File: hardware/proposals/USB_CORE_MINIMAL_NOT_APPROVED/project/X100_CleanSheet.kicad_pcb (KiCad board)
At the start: 4 copper layers, 45 x 45 mm, 240 parts, among them J401 124019772112A, J501 1040310811, J601 SM04B-GHS-TB(LF)(SN), J701 SM06B-GHS-TB(LF)(SN), J702 SM06B-GHS-TB(LF)(SN), J703 SM06B-GHS-TB(LF)(SN), J704 SM04B-GHS-TB(LF)(SN), J801 OUT1 /GND, J802 OUT2 /GND, J803 OUT3 /GND, J804 OUT4 /GND, J805 OUT5 /GND, J806 OUT6 /GND, J807 SWD:1REF2GND3IO4CLK5NRST, J808 BATTERY/bench3S-6S ONLY, J809 CURRENT monitor only, Q101 DMP6023LSS-13, Q102 BSS138LT1G CAN shutdown, U101 TPS54360BDDAR, U102 AP63203WU-7, U103 TPS7A2033PDBVR, U104 TPS2553DBVR, U105 TPS2116DRLR, U106 TPS2553DBVR, U107 TPS22918DBVR core controlled 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, U108 TPS22918DBVR, U109 SN74CB3Q3245PWR, U110 TLV6700DDCR, U111 SN74LVC1G00DBVR, U112 TMUX1219DBVR ILIM selector, U114 SN74AUP1G32DBVR core sensor EN, U201 STM32H743VIT6, U301 BMI088, U302 SPL06-001, U401 TPD2E2U06QDBZRQ1, U402 SN74LVC1G17DBVR, U403 TPD2E2U06QDBZRQ1, U404 TPD2E2U06QDBZRQ1, U601 TCAN3414DR, U801 TMUX1511PWR, Y201 8.000MHz /CL20pF

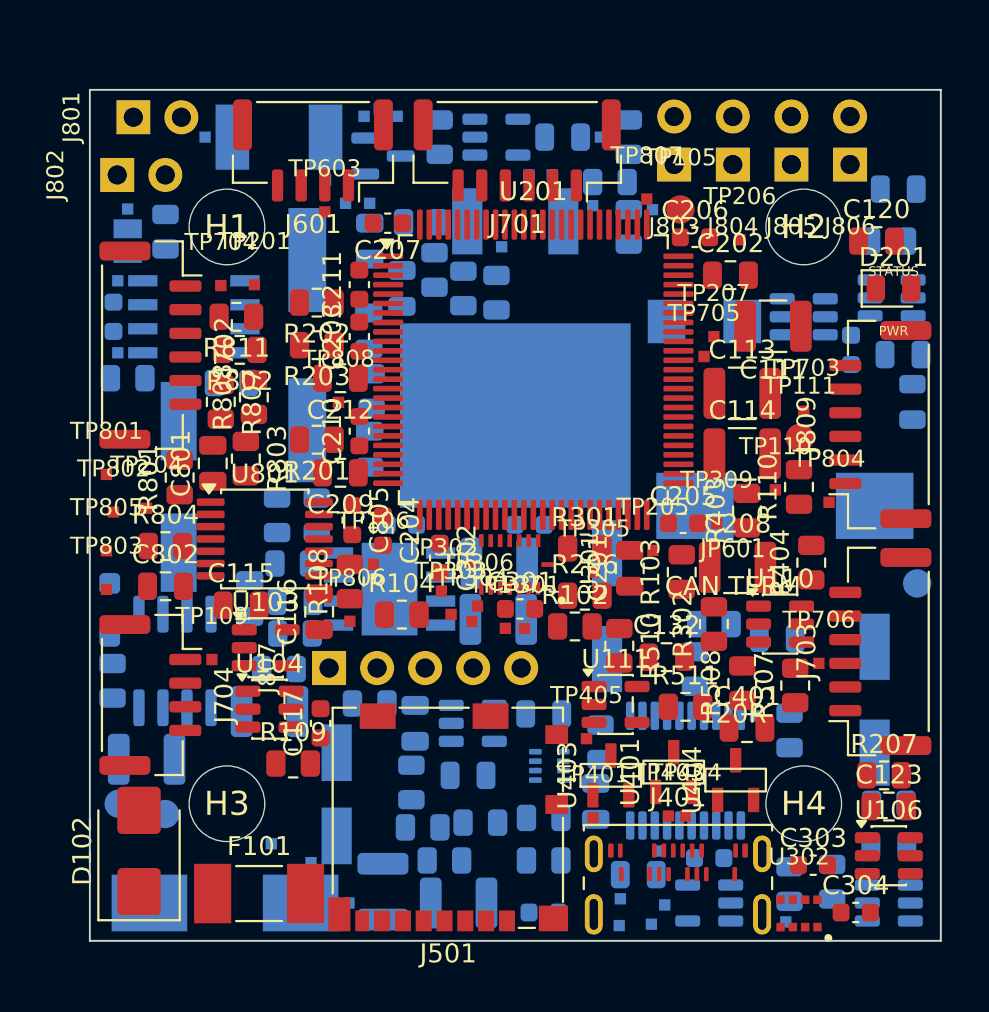
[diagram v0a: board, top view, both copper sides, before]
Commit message: Clear all four 7mm mounting envelopes in the complete USB layout
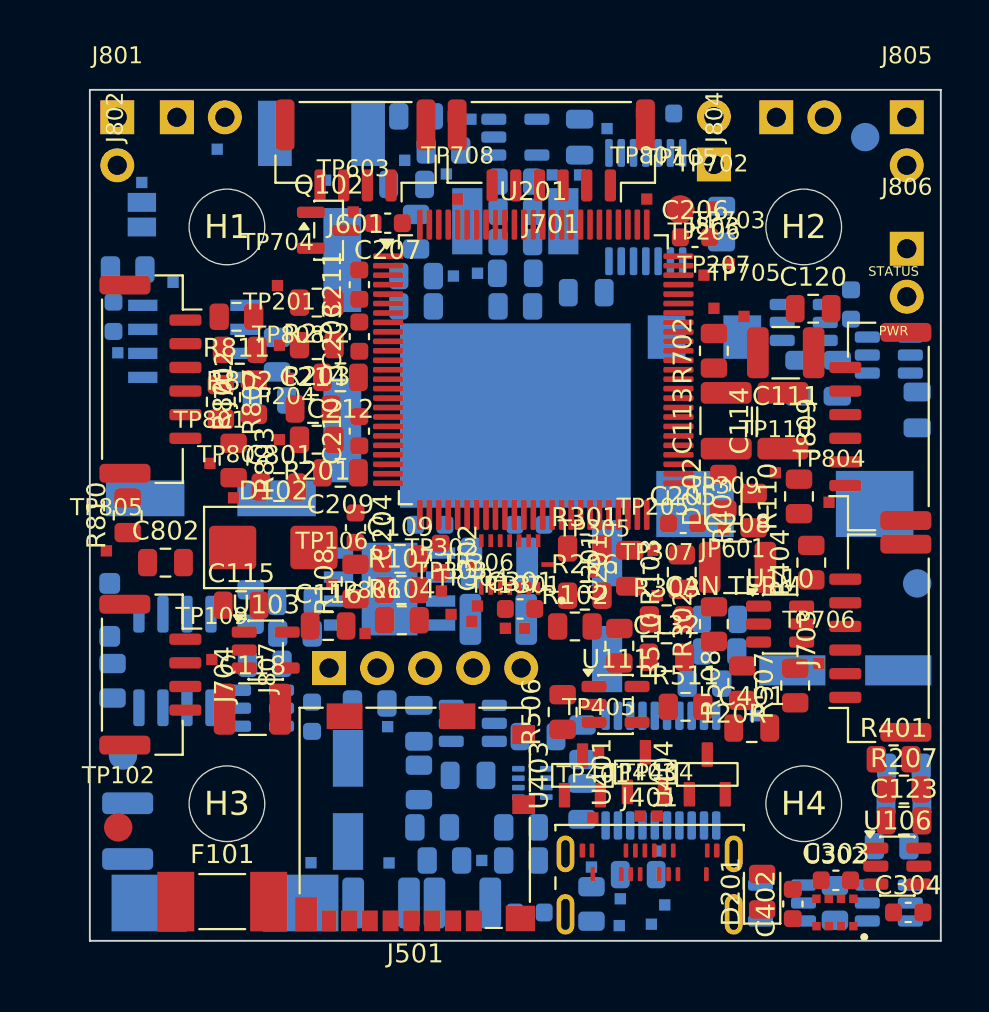
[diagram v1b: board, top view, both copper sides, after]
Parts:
- C109, C118, C214, C402, D202, Q102, R107, R303, R401, R506, R702, R810, TP102, TP307, TP702, TP708: moved to F.Cu
- C117, C202, C805, R109, R804, R808, TP111, TP803, U104, U801: moved to B.Cu
- moved R304 35.9 mm to (104.0, 120.5)
- moved TP308 34.9 mm to (104.0, 118.6)
- moved D201 32.6 mm to (113.0, 119.9), turned to 90 degrees
- moved C805 26.9 mm to (107.6, 78.8), turned to 180 degrees
- moved U801 26.7 mm to (106.9, 83.7), turned to 90 degrees
- moved TP803 25.8 mm to (98.0, 87.2)
- moved R804 25.6 mm to (100.0, 84.0)
- moved R303 25.6 mm to (108.0, 105.5), turned to 0 degrees
- moved R810 22.8 mm to (79.5, 100.0)
- moved TP307 18.5 mm to (107.5, 104.2)
- moved D102 17.6 mm to (87.2, 101.7), turned to 0 degrees
- moved R805 16.7 mm to (94.8, 85.0)
- moved TP111 16.3 mm to (118.5, 80.0)
- moved R702 15.4 mm to (110.5, 91.3)
- moved R808 14.6 mm to (100.0, 89.0), turned to 0 degrees
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
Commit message: Clear MCU-IMU routing channel in the complete USB candidate
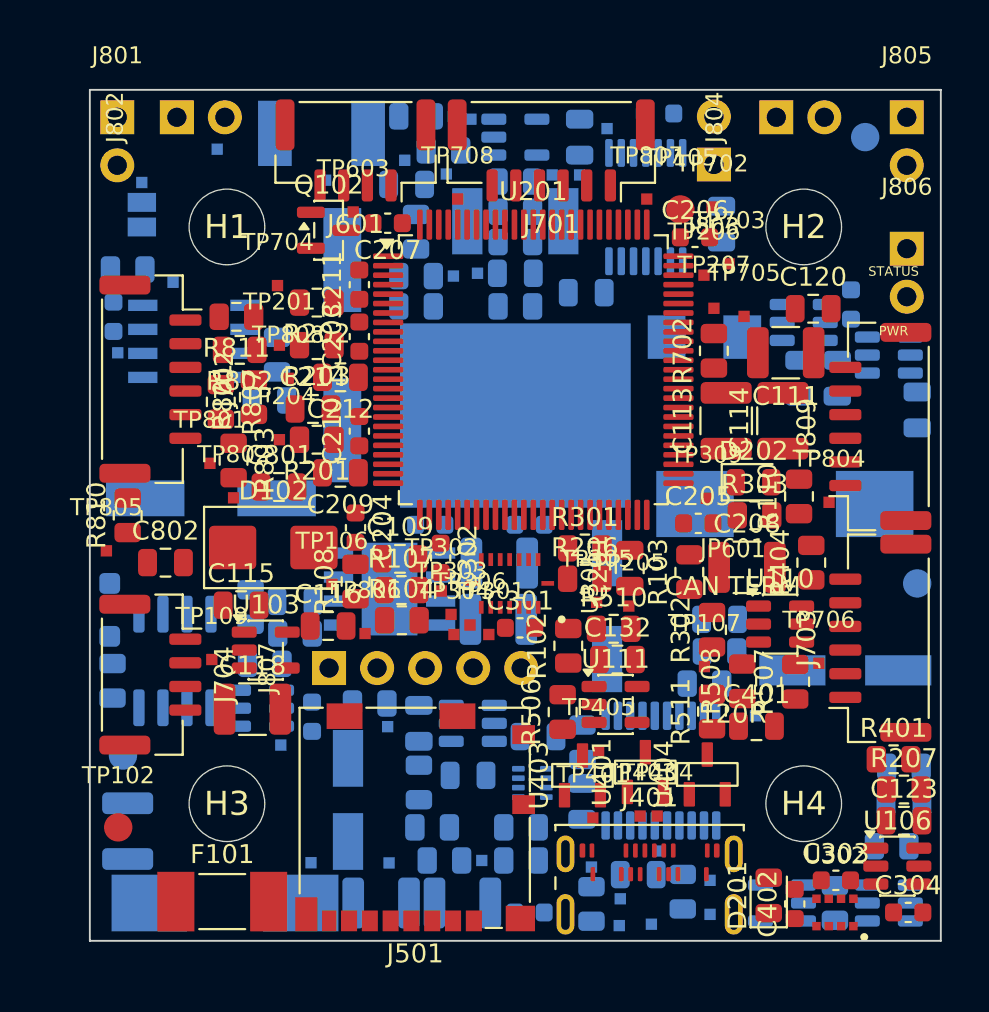
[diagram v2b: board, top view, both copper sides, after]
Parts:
- R403, TP110, TP307: moved to B.Cu
- moved TP110 29.9 mm to (87.6, 112.2)
- moved R403 20.5 mm to (108.8, 119.9)
- moved TP307 15.3 mm to (110.3, 119.3)
- moved TP107 10.7 mm to (110.0, 108.0)
- moved R303 7.20 mm to (112.7, 100.0)
- moved TP205 3.21 mm to (106.0, 104.8)
- moved C132 2.60 mm to (105.4, 107.6)
- moved TP402 2.45 mm to (110.3, 121.1)
- moved TP301 1.90 mm to (98.6, 106.3)
- moved TP309 1.86 mm to (110.1, 99.1)
- moved D202 1.68 mm to (112.6, 98.2), turned to 0 degrees
- moved TP305 1.61 mm to (104.3, 104.6)
- moved R511 1.42 mm to (110.4, 110.4), turned to 90 degrees
- moved TP304 1.18 mm to (96.8, 106.3)
- moved R102 1.08 mm to (102.8, 106.9), turned to 90 degrees
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
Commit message: Route main Buck controls and ground in the unified X100 candidate
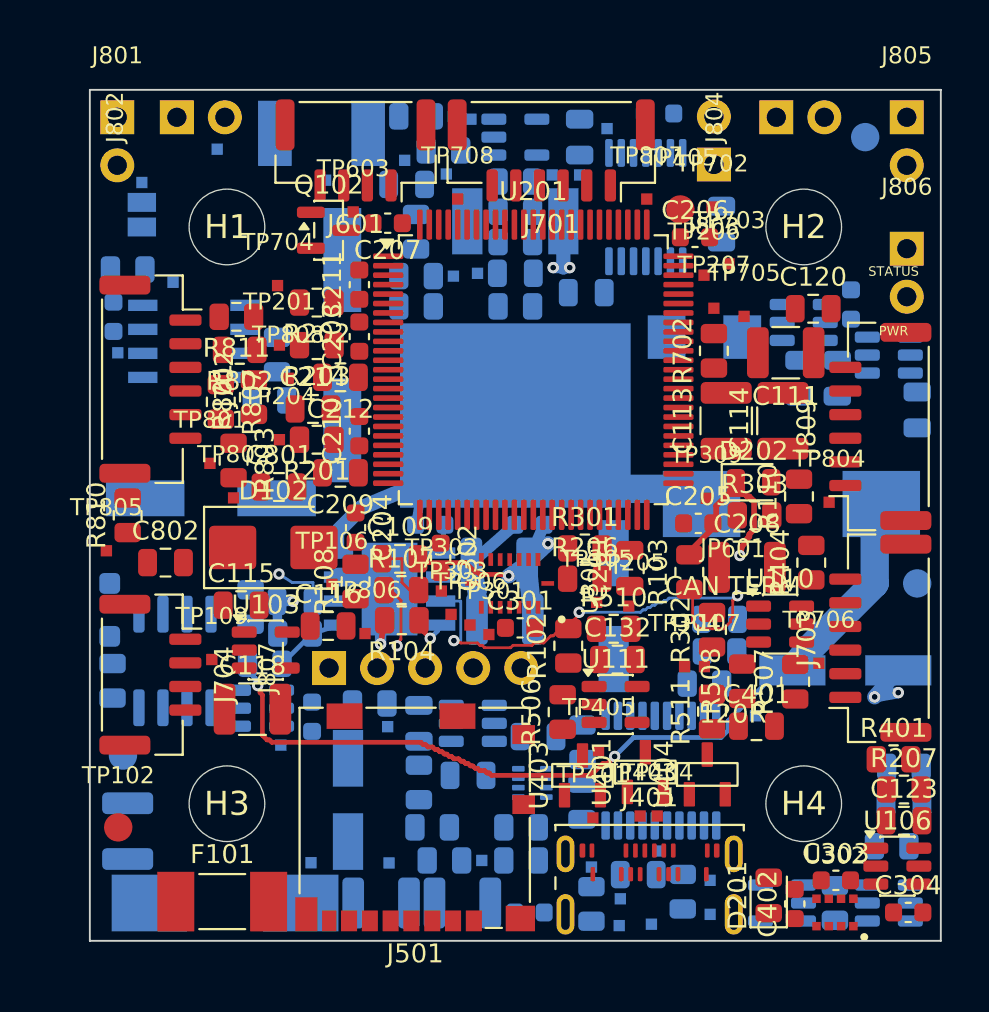
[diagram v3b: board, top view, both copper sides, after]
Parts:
- moved TP304 12.3 mm to (109.0, 108.0)
- moved C102 0.35 mm to (99.5, 105.5)
- moved C121 0.35 mm to (105.2, 104.8)
- moved L101 0.35 mm to (114.6, 99.4)
- turned R104 to 180 degrees
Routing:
- net 5V_MAIN: track 0.00 -> 46.1 mm, vias 0 -> 2
- net GND: track 0.00 -> 35.7 mm, vias 0 -> 9
- net MAIN_EN: track 0.00 -> 25.5 mm, vias 0 -> 3
- net MAIN_COMP: track 0.00 -> 15.9 mm, vias 0 -> 2
- net MAIN_SW: track 0.00 -> 11.8 mm
- net VBAT_PROTECTED: track 0.00 -> 7.86 mm
- net MAIN_FB: track 0.00 -> 3.72 mm
- net MAIN_COMP_RC: track 0.00 -> 3.35 mm
- net MAIN_RT: track 0.00 -> 2.06 mm, vias 0 -> 1
- net MAIN_BOOT: track 0.00 -> 1.51 mm
- added copper zone on In1.Cu, net GND

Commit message: Connect the X100 protected battery input and verify its copper plane
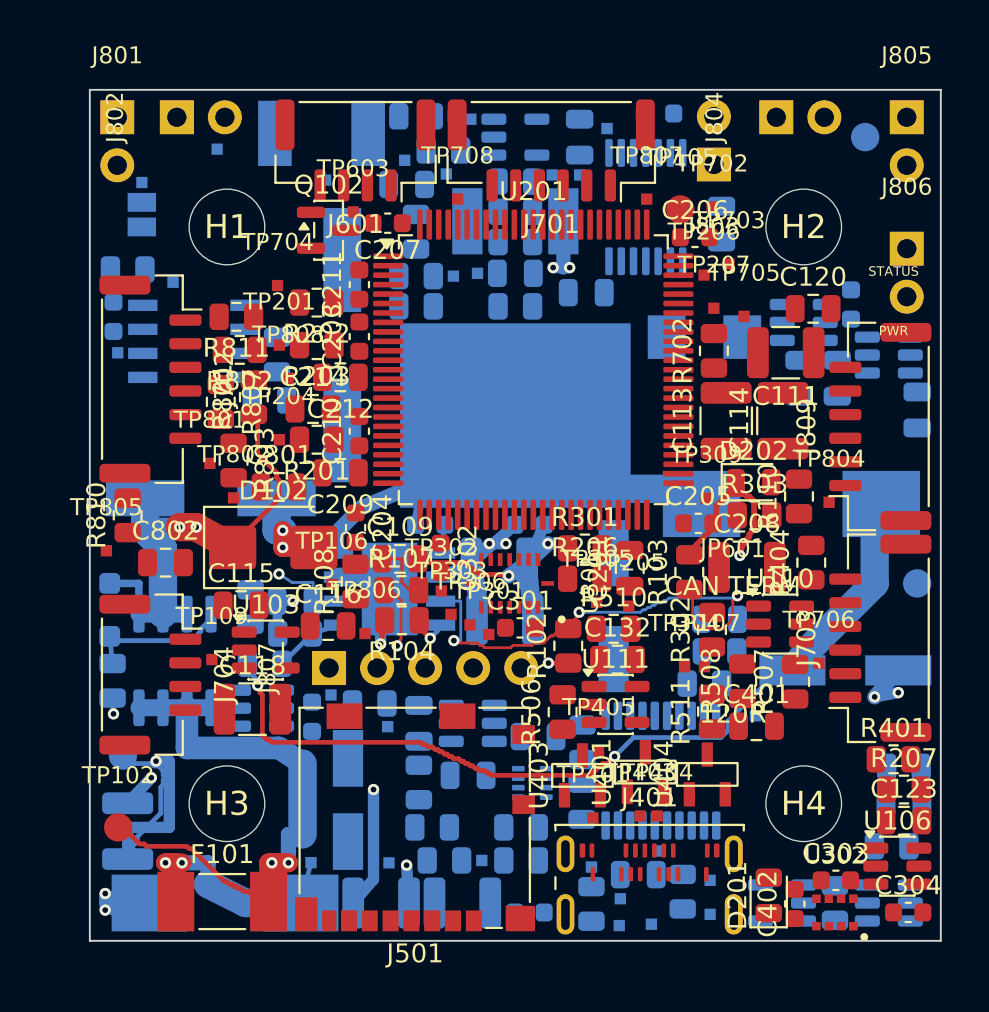
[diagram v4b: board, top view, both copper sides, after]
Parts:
- moved TP101 4.13 mm to (89.2, 118.4)
- moved TP507 4.13 mm to (93.3, 118.4)
- moved TP110 3.75 mm to (90.2, 109.5)
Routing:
- net VBAT_PROTECTED: track 7.86 -> 61.0 mm, vias 0 -> 7
- net VBAT_FUSED: track 0.00 -> 32.7 mm, vias 0 -> 2
- net VBAT_RAW: track 0.00 -> 15.1 mm, vias 0 -> 2
- net GND: track 35.7 -> 48.7 mm, vias 9 -> 16
- net RP_GATE: track 0.00 -> 7.70 mm
- added copper zone on In2.Cu, net VBAT_PROTECTED

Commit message: Route 5V main distribution and preserve isolated feedback sense
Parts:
- R510: moved to B.Cu
- moved R510 10.2 mm to (107.0, 96.0), turned to 90 degrees
- moved R506 5.16 mm to (105.2, 106.0), turned to 0 degrees
- turned C118 to 180 degrees
- turned U104 to 180 degrees
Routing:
- net 5V_MAIN: track 46.1 -> 120.9 mm, vias 2 -> 9
- net CORE_PWR_PRIORITY: track 0.00 -> 13.5 mm
- net GND: track 48.7 -> 58.8 mm, vias 16 -> 21

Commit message: Route external 5V protection and restore input copper capacity
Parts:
- TP110: moved to F.Cu
- moved TP110 12.8 mm to (103.0, 108.8), turned to 180 degrees
- moved R105 0.38 mm to (86.4, 107.8)
- turned R109 to -90 degrees
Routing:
- net EXT_SWITCH_OUT: track 0.00 -> 54.6 mm, vias 0 -> 5
- net EXT_FAULT: track 0.00 -> 37.3 mm, vias 0 -> 3
- net EXT_ILIM: track 0.00 -> 10.6 mm, vias 0 -> 2
- net GND: track 58.8 -> 65.6 mm
- net MAIN_COMP: track 15.9 -> 12.3 mm
- net 5V_MAIN: track 120.9 -> 122.8 mm, vias 9 -> 10
- net MAIN_FB: track 3.72 -> 5.13 mm

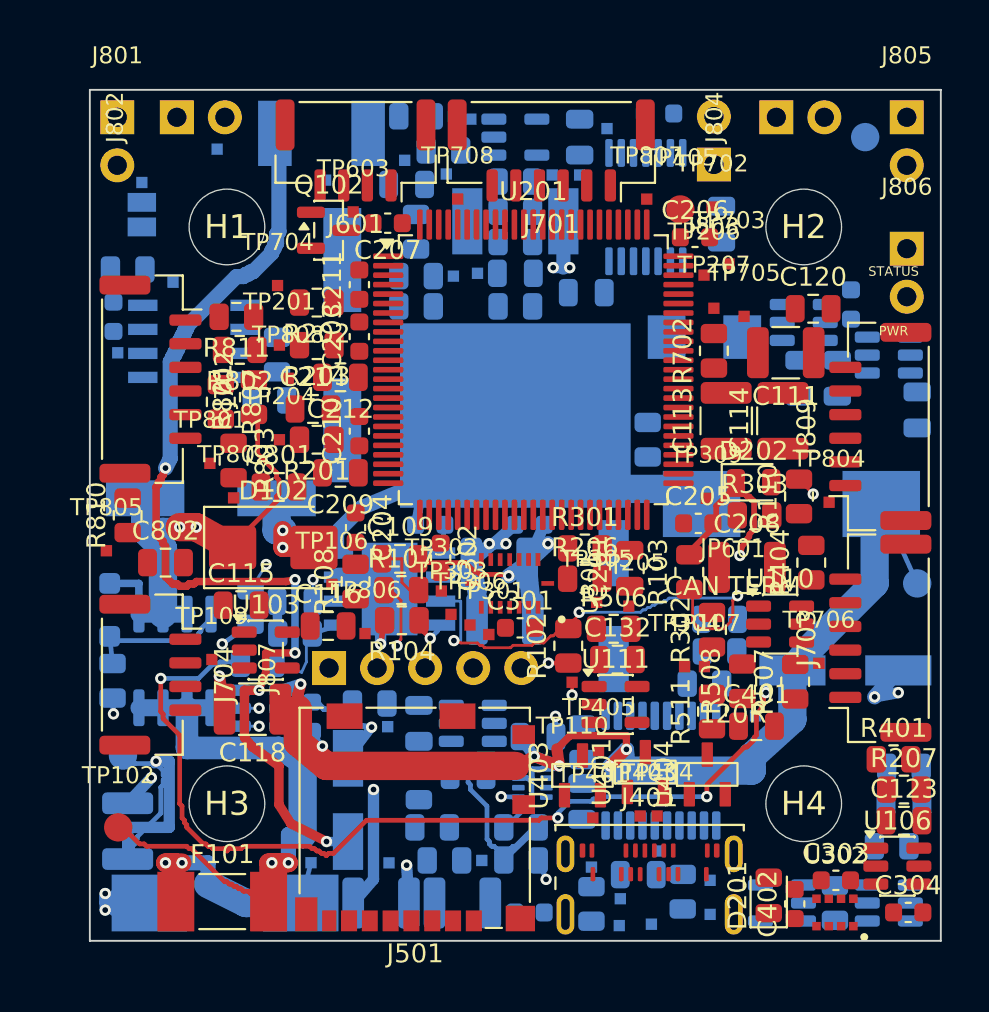
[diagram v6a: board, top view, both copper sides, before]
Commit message: Route core power mux and local 3V3 regulator supply
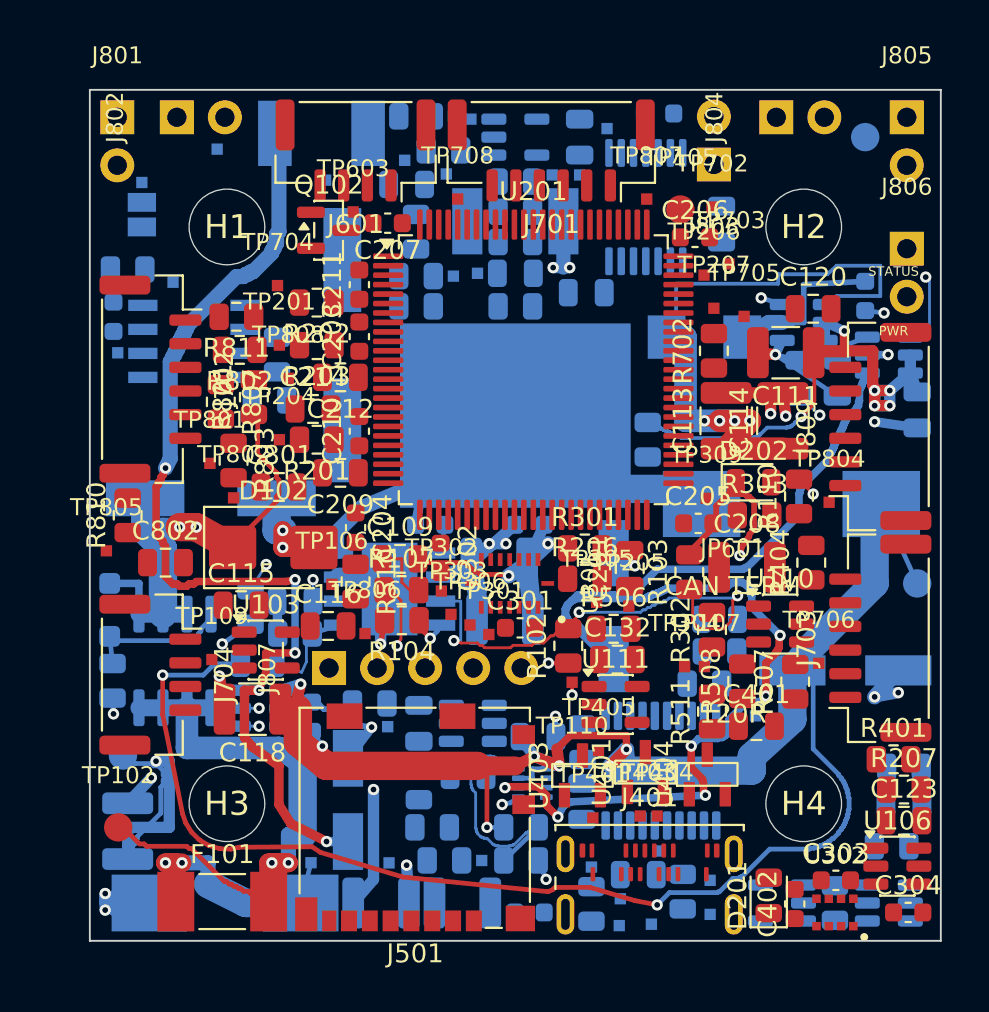
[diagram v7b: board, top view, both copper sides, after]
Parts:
- R108: moved to B.Cu
- R510: moved to F.Cu
- moved R108 17.2 mm to (107.0, 96.0), turned to -90 degrees
- moved R510 17.2 mm to (91.5, 103.5), turned to -90 degrees
- moved C112 0.87 mm to (118.5, 88.4)
- turned U102 to 180 degrees
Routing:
- net 5V_CORE_MUX: track 0.00 -> 74.8 mm, vias 0 -> 6
- net 3V3_MCU: track 0.00 -> 35.6 mm, vias 0 -> 4
- net 5V_CORE: track 0.00 -> 31.8 mm, vias 0 -> 6
- net GND: track 65.6 -> 82.0 mm, vias 21 -> 27
- net CORE_SLEW: track 0.00 -> 15.7 mm, vias 0 -> 2
- net MCU_BOOT: track 0.00 -> 8.72 mm, vias 0 -> 2
- net MCU_SW: track 0.00 -> 8.70 mm
- net 5V_MAIN: track 122.8 -> 131.2 mm, vias 10 -> 9

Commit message: Route first MCU supply pass and expose remaining power islands
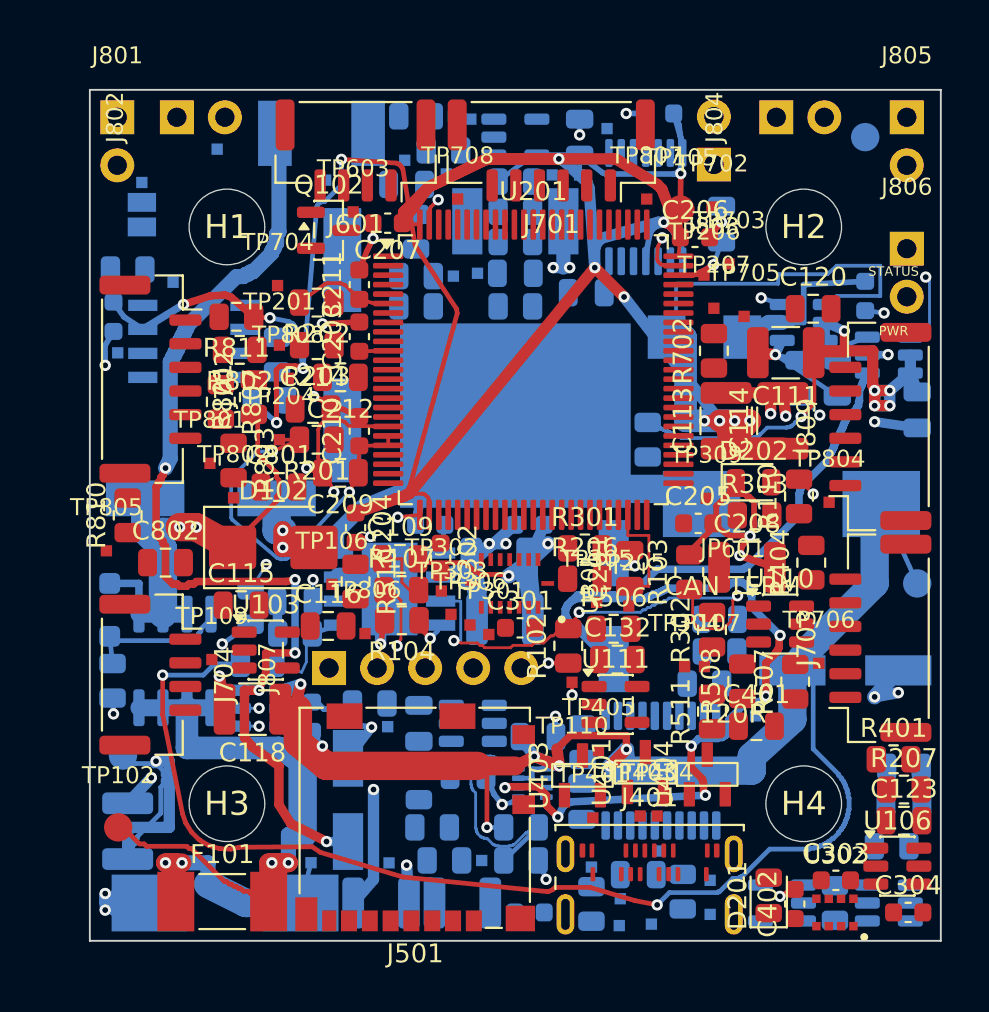
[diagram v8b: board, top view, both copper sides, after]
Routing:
- net 3V3_MCU: track 35.6 -> 206.5 mm, vias 4 -> 14
- net GND: track 82.0 -> 116.8 mm, vias 27 -> 42
- net MCU_VDDA: track 0.00 -> 20.7 mm, vias 0 -> 2
- net VCAP1: track 0.00 -> 6.95 mm
- net MCU_VBAT_3V3: track 0.00 -> 5.37 mm
- net VCAP2: track 0.00 -> 4.61 mm, vias 0 -> 1
